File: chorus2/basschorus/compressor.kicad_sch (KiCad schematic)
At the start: 16 parts, among them U9 TL074

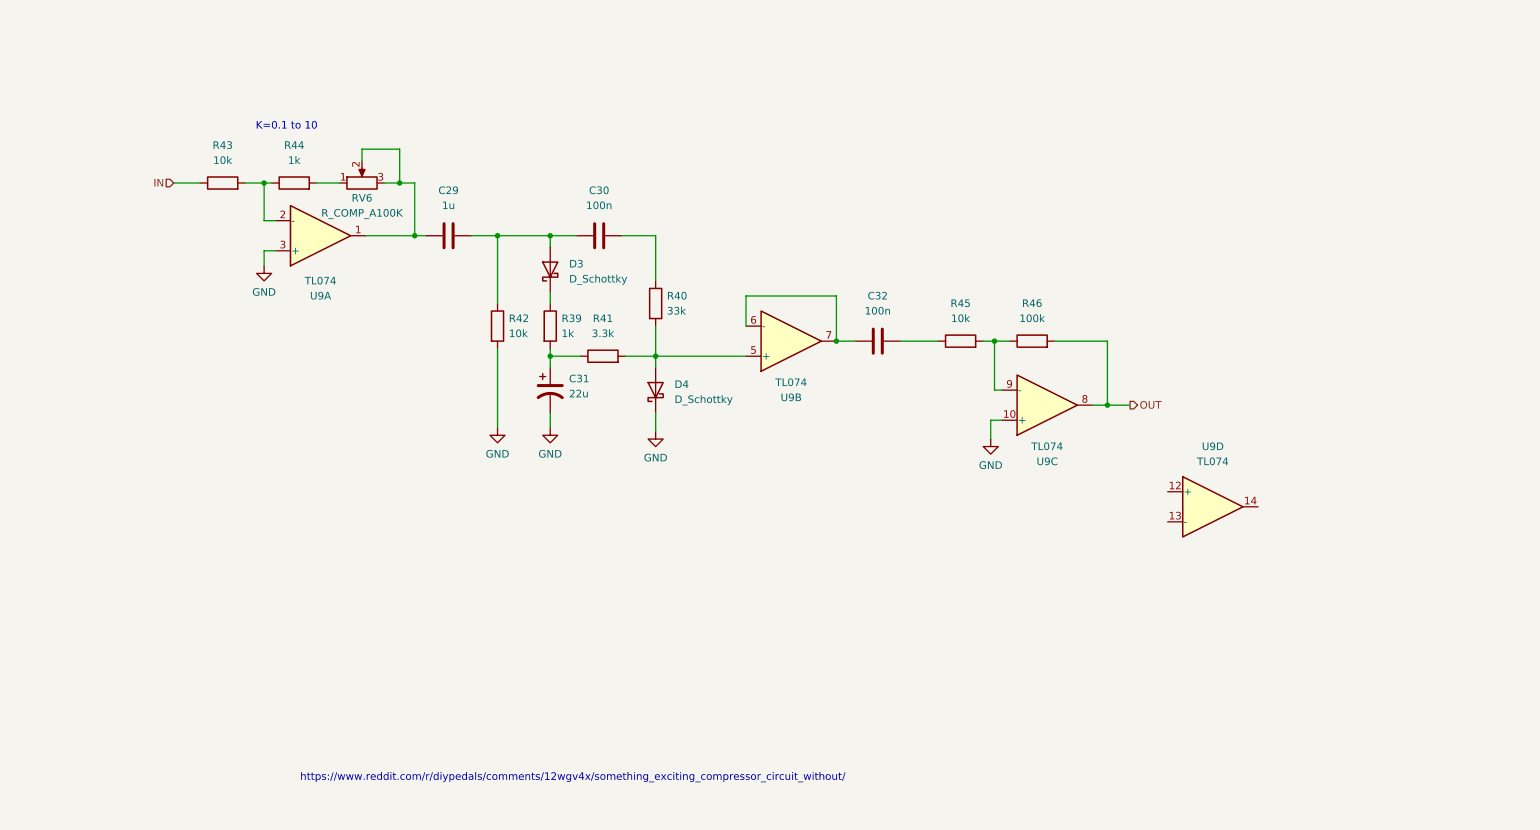
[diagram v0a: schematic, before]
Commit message: update designs based on new calculations
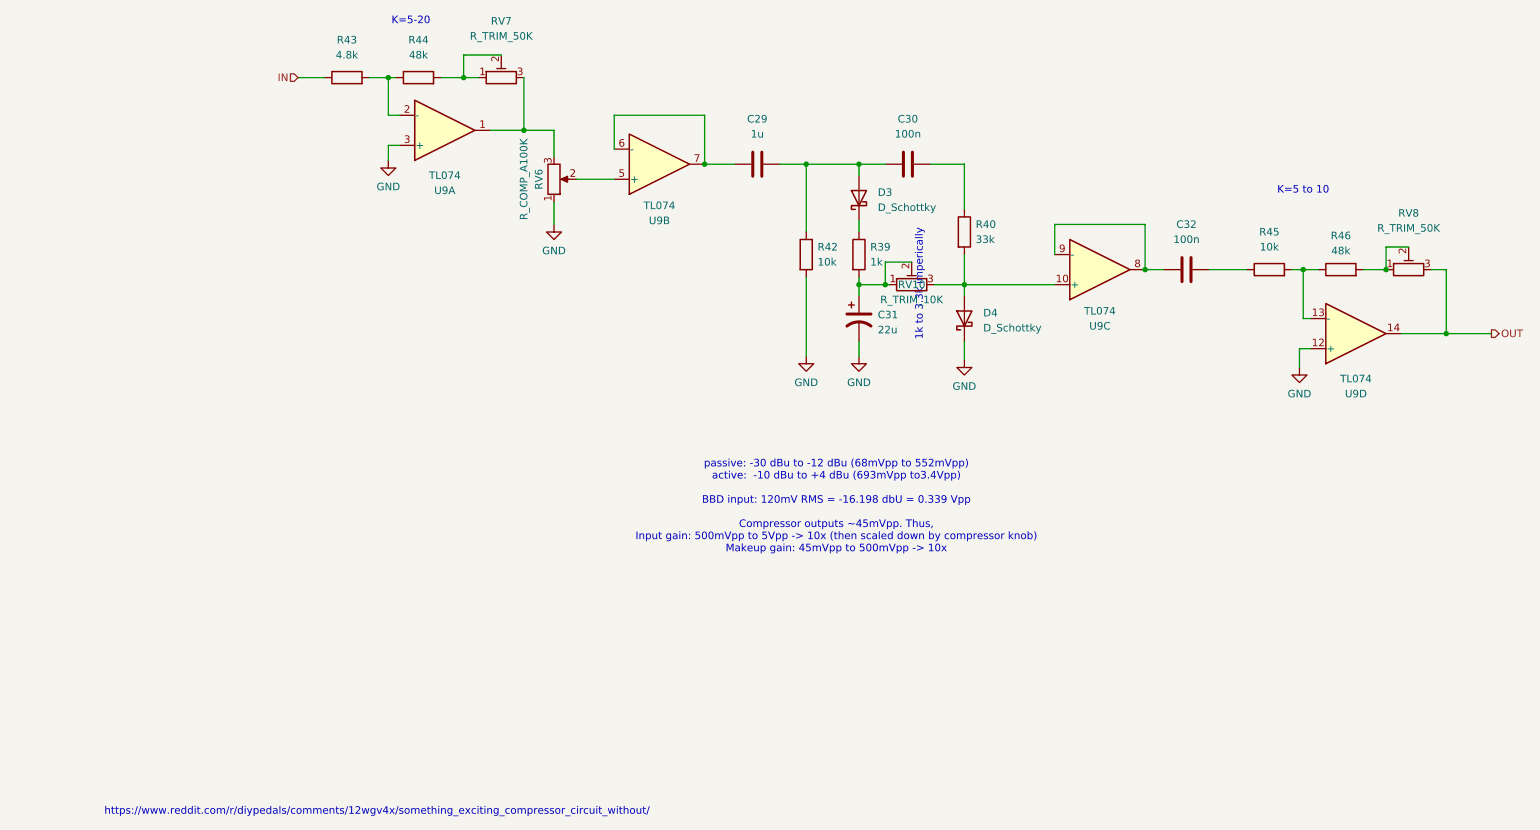
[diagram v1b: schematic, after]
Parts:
- removed R41: 3.3k, symbol Device:R
- added RV10: R_TRIM_10K, symbol Device:R_Potentiometer_Trim
- added RV7, RV8: R_TRIM_50K, symbol Device:R_Potentiometer_Trim
- R43: value 10k -> 4.8k
- R44: value 1k -> 48k
- R46: value 100k -> 48k
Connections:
- net GND: now also RV6.1, U9.12 (+); no longer U9.10 (+)
- net OUT: now also U9.14, RV8.3; no longer R46.2, U9.8
- net at R45.2, R46.1: now also U9.13 (-); no longer U9.9 (-)
- net at R44.2: now also RV7.1, RV7.2; no longer RV6.1
- net at RV6.3, U9.1: now also RV7.3; no longer C29.1, RV6.2
- net at D4.2 (A), R40.2: now also U9.10 (+), RV10.3; no longer U9.5 (+)
- net at U9.6 (-), U9.7: now also C29.1; no longer C32.1
- net at C31.1, R39.2: now also RV10.1, RV10.2
- new net: C32.1, U9.8, U9.9 (-)
- new net: R46.2, RV8.1, RV8.2
- new net: RV6.2, U9.5 (+)
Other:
- note added: "1k to 3.3k imperically"
- note added: "K=5 to 10"
- note added: "K=5-20"
- note added: "passive: -30 dBu to -12 dBu (68mVpp to 552mVpp) active: -10 dBu to +4 dBu (693mVpp to3.4Vpp) BBD input: 120mV RMS = -16.198 dbU = 0.339 Vpp Compressor outputs ~45mVpp. Thus, Input gain: 500mVpp to 5Vpp -> 10x (then scaled down by compressor knob) Makeup gain: 45mVpp to 500mVpp -> 10x"
- note removed: "K=0.1 to 10"
- moved on the sheet: C29, C30, C31, C32, D3, D4, R39, R40, R42, R43, R44, R45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

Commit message: assign parts for testing
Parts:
- added TP10, TP7, TP8, TP9: TestPoint, TestPoint:TestPoint_THTPad_2.5x2.5mm_Drill1.2mm, symbol Connector:TestPoint
- C33: renamed from C29; footprint (none) -> Capacitor_THT:C_Rect_L7.0mm_W2.5mm_P5.00mm
- C34: renamed from C31; footprint (none) -> Capacitor_THT:CP_Radial_D8.0mm_P5.00mm
- C35: renamed from C30; footprint (none) -> Capacitor_THT:C_Rect_L7.0mm_W2.5mm_P5.00mm
- C36: renamed from C32; footprint (none) -> Capacitor_THT:C_Rect_L7.0mm_W2.5mm_P5.00mm
- D3, D4: footprint (none) -> Diode_THT:D_DO-34_SOD68_P7.62mm_Horizontal
- R41: renamed from R43; footprint (none) -> Resistor_THT:R_Axial_DIN0204_L3.6mm_D1.6mm_P5.08mm_Horizontal
- R42: renamed from R44; footprint (none) -> Resistor_THT:R_Axial_DIN0204_L3.6mm_D1.6mm_P5.08mm_Horizontal
- R43: renamed from R42; footprint (none) -> Resistor_THT:R_Axial_DIN0204_L3.6mm_D1.6mm_P5.08mm_Horizontal
- R44: renamed from R39; footprint (none) -> Resistor_THT:R_Axial_DIN0204_L3.6mm_D1.6mm_P5.08mm_Horizontal
- R45: renamed from R40; footprint (none) -> Resistor_THT:R_Axial_DIN0204_L3.6mm_D1.6mm_P5.08mm_Horizontal
- R46: renamed from R45; footprint (none) -> Resistor_THT:R_Axial_DIN0204_L3.6mm_D1.6mm_P5.08mm_Horizontal
- R47: renamed from R46; footprint (none) -> Resistor_THT:R_Axial_DIN0204_L3.6mm_D1.6mm_P5.08mm_Horizontal
- RV10: footprint (none) -> Potentiometer_THT:Potentiometer_Vishay_T73YP_Vertical
- RV11: renamed from RV8; footprint (none) -> Potentiometer_THT:Potentiometer_Vishay_T73YP_Vertical
- RV8: renamed from RV7; footprint (none) -> Potentiometer_THT:Potentiometer_Vishay_T73YP_Vertical
- RV9: renamed from RV6; footprint (none) -> Potentiometer_THT:Potentiometer_Alpha_RD901F-40-00D_Single_Vertical_CircularHoles
- U3: renamed from U9; footprint (none) -> Package_SO:SO-14_3.9x8.65mm_P1.27mm
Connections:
- net at C36.1, U3.8, U3.9 (-): now also TP9.1
- net at RV8.3, RV9.3, U3.1: now also TP7.1
- net at C33.1, U3.6 (-), U3.7: now also TP8.1
- net at C34.1, R44.2, RV10.1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: now also TP10.1

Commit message: started layout
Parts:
- TP10: value TestPoint -> ENV
- TP7: value TestPoint -> COMP_GAIN
- TP8: value TestPoint -> COMP_IN
- TP9: value TestPoint -> COMP_OUT
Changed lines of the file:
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@@
 			)
 		)
-		(property "Value" "TestPoint"
+		(property "Value" "COMP_IN"
 			(at 125.73 86.4869 0)
 			(effects
@@
 			)
 		)
-		(property "Value" "TestPoint"
+		(property "Value" "COMP_GAIN"
 			(at 100.33 74.1679 0)
 			(effects
@@
 			)
 		)
-		(property "Value" "TestPoint"
+		(property "Value" "COMP_OUT"
 			(at 199.39 104.2669 0)
 			(effects
@@
 		(fields_autoplaced yes)
 		(property "Reference" "TP10"
-			(at 145.923 97.155 90)
-			(effects
-				(font
-					(size 1.27 1.27)
-				)
-			)
-		)
-		(property "Value" "TestPoint"
-			(at 145.923 99.695 90)
-			(effects
-				(font
+			(at 145.923 96.52 90)
+			(effects
+				(font
+					(size 1.27 1.27)
+				)
+			)
+		)
+		(property "Value" "ENV"
+			(at 145.923 99.06 90)
+			(effects
+				(font

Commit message: basic layout
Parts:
- R41, R42, R43, R44, R45, R46, R47: footprint Resistor_THT:R_Axial_DIN0204_L3.6mm_D1.6mm_P5.08mm_Horizontal -> Resistor_THT:R_Axial_DIN0204_L3.6mm_D1.6mm_P2.54mm_Vertical
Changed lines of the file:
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@@
 			)
 		)
-		(property "Footprint" "Resistor_THT:R_Axial_DIN0204_L3.6mm_D1.6mm_P5.08mm_Horizontal"
+		(property "Footprint" "Resistor_THT:R_Axial_DIN0204_L3.6mm_D1.6mm_P2.54mm_Vertical"
 			(at 74.93 69.088 90)
 			(effects
@@
 			)
 		)
-		(property "Footprint" "Resistor_THT:R_Axial_DIN0204_L3.6mm_D1.6mm_P5.08mm_Horizontal"
+		(property "Footprint" "Resistor_THT:R_Axial_DIN0204_L3.6mm_D1.6mm_P2.54mm_Vertical"
 			(at 230.505 101.473 90)
 			(effects
@@
 			)
 		)
-		(property "Footprint" "Resistor_THT:R_Axial_DIN0204_L3.6mm_D1.6mm_P5.08mm_Horizontal"
+		(property "Footprint" "Resistor_THT:R_Axial_DIN0204_L3.6mm_D1.6mm_P2.54mm_Vertical"
 			(at 62.865 69.088 90)
 			(effects
@@
 			)
 		)
-		(property "Footprint" "Resistor_THT:R_Axial_DIN0204_L3.6mm_D1.6mm_P5.08mm_Horizontal"
+		(property "Footprint" "Resistor_THT:R_Axial_DIN0204_L3.6mm_D1.6mm_P2.54mm_Vertical"
 			(at 138.557 97.155 90)
 			(effects
@@
 			)
 		)
-		(property "Footprint" "Resistor_THT:R_Axial_DIN0204_L3.6mm_D1.6mm_P5.08mm_Horizontal"
+		(property "Footprint" "Resistor_THT:R_Axial_DIN0204_L3.6mm_D1.6mm_P2.54mm_Vertical"
 			(at 147.447 97.155 90)
 			(effects
@@
 			)
 		)
-		(property "Footprint" "Resistor_THT:R_Axial_DIN0204_L3.6mm_D1.6mm_P5.08mm_Horizontal"
+		(property "Footprint" "Resistor_THT:R_Axial_DIN0204_L3.6mm_D1.6mm_P2.54mm_Vertical"
 			(at 165.227 93.345 90)
 			(effects
@@
 			)
 		)
-		(property "Footprint" "Resistor_THT:R_Axial_DIN0204_L3.6mm_D1.6mm_P5.08mm_Horizontal"
+		(property "Footprint" "Resistor_THT:R_Axial_DIN0204_L3.6mm_D1.6mm_P2.54mm_Vertical"
 			(at 218.44 101.473 90)
 			(effects

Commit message: cleanup
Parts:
- TP7: value COMP_GAIN -> CGAIN
- TP8: value COMP_IN -> CIN
- TP9: value COMP_OUT -> COUT
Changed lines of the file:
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@@
 			)
 		)
-		(property "Value" "COMP_IN"
+		(property "Value" "CIN"
 			(at 125.73 86.4869 0)
 			(effects
@@
 			)
 		)
-		(property "Value" "COMP_GAIN"
+		(property "Value" "CGAIN"
 			(at 100.33 74.1679 0)
 			(effects
@@
 			)
 		)
-		(property "Value" "COMP_OUT"
+		(property "Value" "COUT"
 			(at 199.39 104.2669 0)
 			(effects
